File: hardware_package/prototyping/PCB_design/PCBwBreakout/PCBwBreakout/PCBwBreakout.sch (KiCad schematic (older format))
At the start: 4 parts

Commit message: Fixed Schematic frame & title, added Lora Headers
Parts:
- added ? (x2), U?: VIN, symbol PCBwBreakout-eagle-import:VIN
- added JP?: HEADER-1X5, symbol PCBwBreakout-eagle-import:HEADER-1X5
- added JP?: HEADER-1X9, symbol PCBwBreakout-eagle-import:HEADER-1X9
- added R? (x2): 100k, symbol Device:R
- ?: symbol PCBwBreakout-eagle-import:VBAT -> PCBwBreakout-rescue:VBAT-PCBwBreakout-eagle-import
- ?: symbol PCBwBreakout-eagle-import:VBUS -> PCBwBreakout-rescue:VBUS-PCBwBreakout-eagle-import
- JP?: symbol PCBwBreakout-eagle-import:HEADER-1X12 -> PCBwBreakout-rescue:HEADER-1X12-PCBwBreakout-eagle-import
- JP?: symbol PCBwBreakout-eagle-import:HEADER-1X16 -> PCBwBreakout-rescue:HEADER-1X16-PCBwBreakout-eagle-import
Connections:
- net labels added: CS_5V, DIO0, DIO1, DIO2, DIO3, DIO4, DIO5, MISO_3V, MOSI_5V, RST_5V, SCK_5V
- wire segments 30 -> 48
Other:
- note added: "RFM69HCW\n"
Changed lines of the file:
@@
 $EndDescr
 $Comp
-L PCBwBreakout-eagle-import:HEADER-1X12 JP?
+L PCBwBreakout-rescue:HEADER-1X12-PCBwBreakout-eagle-import JP?
 U 1 1 5F621D11
 P 1700 1750
@@
 $EndComp
 $Comp
-L PCBwBreakout-eagle-import:HEADER-1X16 JP?
+L PCBwBreakout-rescue:HEADER-1X16-PCBwBreakout-eagle-import JP?
 U 1 1 5F62456E
 P 3200 1800
@@
 	1600 2150 1100 2150
 $Comp
-L PCBwBreakout-eagle-import:VBAT ?
+L PCBwBreakout-rescue:VBAT-PCBwBreakout-eagle-import ?
 U 1 1 5F62F850
 P 900 1150
@@
 $EndComp
 $Comp
-L PCBwBreakout-eagle-import:VBUS ?
+L PCBwBreakout-rescue:VBUS-PCBwBreakout-eagle-import ?
 U 1 1 5F630C46
 P 900 1350
@@
 Wire Notes Line
 	500  3100 4100 3100
-Wire Notes Line
-	4100 3100 4100 500
 Text Notes 600  600  0    71   ~ 0
 Feather Headers\n
+$Comp
+L PCBwBreakout-eagle-import:HEADER-1X5 JP?
+U 1 1 5F60BB99
+P 1750 4000
+F 0 "JP?" H 1828 4053 59  0000 L CNN
+F 1 "HEADER-1X5" H 1828 3948 59  0000 L CNN
+F 2 "" H 1750 4000 71  0001 C CNN
+F 3 "" H 1750 4000 71  0001 C CNN
+	1    1750 4000
+	1    0    0    -1
+$EndComp
+Wire Wire Line
+	1650 3800 1100 3800
+Wire Wire Line
+	1650 3900 1100 3900
+Wire Wire Line
+	1650 4000 1100 4000
+Wire Wire Line
+	1650 4100 1100 4100
+Wire Wire Line
+	1650 4200 1100 4200
+Text Label 1200 3800 0    71   ~ 0
+DIO1
+Text Label 1200 3900 0    71   ~ 0
+DIO2
+Text Label 1200 4000 0    71   ~ 0
+DIO3
+Text Label 1200 4100 0    71   ~ 0
+DIO4
+Text Label 1200 4200 0    71   ~ 0
+DIO5
+$Comp
+L PCBwBreakout-eagle-import:HEADER-1X9 JP?
+U 1 1 5F613941
+P 3300 3850
+F 0 "JP?" H 3378 3903 59  0000 L CNN
+F 1 "HEADER-1X9" H 3378 3798 59  0000 L CNN
+F 2 "" H 3300 3850 71  0001 C CNN
+F 3 "" H 3300 3850 71  0001 C CNN
+	1    3300 3850
+	1    0    0    -1
+$EndComp
+$Comp
+L PCBwBreakout-eagle-import:VIN ?
+U 1 1 5F61445D
+P 2500 3450
+F 0 "?" H 2550 3500 71  0001 C CNN
+F 1 "VIN" V 2617 3413 42  0000 C CNN
+F 2 "" H 2500 3450 71  0001 C CNN
+F 3 "" H 2500 3450 71  0001 C CNN
+	1    2500 3450
+	0    -1   -1   0
+$EndComp
+Wire Wire Line
+	3200 3450 2600 3450
+$Comp
+L power:GND #PWR?
+U 1 1 5F615E5F
+P 2700 3550
+F 0 "#PWR?" H 2700 3300 50  0001 C CNN
+F 1 "GND" V 2705 3422 50  0000 R CNN
+F 2 "" H 2700 3550 50  0001 C CNN
+F 3 "" H 2700 3550 50  0001 C CNN
+	1    2700 3550
+	0    1    1    0
+$EndComp
+Wire Wire Line
+	3200 3550 2700 3550
+Text Label 2800 3650 0    71   ~ 0
+EN
+Text Label 2750 3750 0    71   ~ 0
+DIO0
+Text Label 2650 3850 0    71   ~ 0
+SCK_5V
+Text Label 2600 3950 0    71   ~ 0
+MISO_3V
+Wire Wire Line
+	2550 3950 3200 3950
+Wire Wire Line
+	2550 3850 3200 3850
+Wire Wire Line
+	2550 3750 3200 3750
+Wire Wire Line
+	2550 3650 3200 3650
+Wire Wire Line
+	2550 4050 3200 4050
+Text Label 2600 4050 0    71   ~ 0
+MOSI_5V
+$Comp
+L Device:R R?
+U 1 1 5F622386
+P 2500 4500
+F 0 "R?" H 2570 4546 50  0000 L CNN
+F 1 "100k" H 2570 4455 50  0000 L CNN
+F 2 "" V 2430 4500 50  0001 C CNN
+F 3 "~" H 2500 4500 50  0001 C CNN
+	1    2500 4500
+	1    0    0    -1
+$EndComp
+$Comp
+L Device:R R?
+U 1 1 5F6265FE
+P 2800 4500
+F 0 "R?" H 2870 4546 50  0000 L CNN
+F 1 "100k" H 2870 4455 50  0000 L CNN
+F 2 "" V 2730 4500 50  0001 C CNN
+F 3 "~" H 2800 4500 50  0001 C CNN
+	1    2800 4500
+	1    0    0    -1
+$EndComp
+Wire Wire Line
+	3200 4150 2500 4150
+Wire Wire Line
+	2500 4150 2500 4350
+Wire Wire Line
+	3200 4250 2800 4250
+Wire Wire Line
+	2800 4250 2800 4350
+$Comp
+L PCBwBreakout-eagle-import:VIN ?
+U 1 1 5F628E28
+P 2500 4850
+F 0 "?" H 2550 4900 71  0001 C CNN
+F 1 "VIN" H 2422 4812 42  0000 R CNN
+F 2 "" H 2500 4850 71  0001 C CNN
+F 3 "" H 2500 4850 71  0001 C CNN
+	1    2500 4850
+	-1   0    0    1
+$EndComp
+$Comp
+L PCBwBreakout-eagle-import:VIN U?
+U 1 1 5F629B04
+P 2800 4850
+F 0 "U?" H 2850 4900 71  0001 C CNN
+F 1 "VIN" H 2722 4812 42  0000 R CNN
+F 2 "" H 2800 4850 71  0001 C CNN
+F 3 "" H 2800 4850 71  0001 C CNN
+	1    2800 4850
+	-1   0    0    1
+$EndComp
+Wire Wire Line
+	2500 4650 2500 4750
+Wire Wire Line
+	2800 4650 2800 4750
+Text Label 2650 4150 0    71   ~ 0
+CS_5V
+Text Label 2800 4250 0    71   ~ 0
+RST_5V
+Wire Notes Line
+	450  5150 4100 5150
+Wire Notes Line
+	4100 500  4100 5150
+Text Notes 550  3250 0    71   ~ 0
+RFM69HCW\n
 $EndSCHEMATC

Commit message: Added GPS headers
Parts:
- added ? (x2): 3.3V, symbol PCBwBreakout-eagle-import:3.3V
- added JP? (x2): HEADER-1X6, symbol PCBwBreakout-eagle-import:HEADER-1X6
- ? (x2), U?: symbol PCBwBreakout-eagle-import:VIN -> PCBwBreakout-rescue:VIN-PCBwBreakout-eagle-import
- JP?: symbol PCBwBreakout-eagle-import:HEADER-1X5 -> PCBwBreakout-rescue:HEADER-1X5-PCBwBreakout-eagle-import
- JP?: symbol PCBwBreakout-eagle-import:HEADER-1X9 -> PCBwBreakout-rescue:HEADER-1X9-PCBwBreakout-eagle-import
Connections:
- net labels added: 1PPS, RXI, TXO, VCC, WAKEUP
- net labels removed: +3V3
- wire segments 48 -> 61
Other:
- note added: "GPS \n"
- note added: "STM32 Adafruit Feather\n\n"
- note removed: "Feather Headers\n"
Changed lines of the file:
@@
 Wire Wire Line
 	3100 2500 2900 2500
-Text Label 2600 2500 0    50   ~ 0
-+3V3
 Wire Wire Line
 	2900 2400 2900 2500
@@
 Wire Notes Line
 	500  3100 4100 3100
-Text Notes 600  600  0    71   ~ 0
-Feather Headers\n
-$Comp
-L PCBwBreakout-eagle-import:HEADER-1X5 JP?
+Text Notes 600  700  0    71   ~ 0
+STM32 Adafruit Feather\n\n
+$Comp
+L PCBwBreakout-rescue:HEADER-1X5-PCBwBreakout-eagle-import JP?
 U 1 1 5F60BB99
 P 1750 4000
@@
 DIO5
 $Comp
-L PCBwBreakout-eagle-import:HEADER-1X9 JP?
+L PCBwBreakout-rescue:HEADER-1X9-PCBwBreakout-eagle-import JP?
 U 1 1 5F613941
 P 3300 3850
@@
 $EndComp
 $Comp
-L PCBwBreakout-eagle-import:VIN ?
+L PCBwBreakout-rescue:VIN-PCBwBreakout-eagle-import ?
 U 1 1 5F61445D
 P 2500 3450
@@
 	2800 4250 2800 4350
 $Comp
-L PCBwBreakout-eagle-import:VIN ?
+L PCBwBreakout-rescue:VIN-PCBwBreakout-eagle-import ?
 U 1 1 5F628E28
 P 2500 4850
@@
 $EndComp
 $Comp
-L PCBwBreakout-eagle-import:VIN U?
+L PCBwBreakout-rescue:VIN-PCBwBreakout-eagle-import U?
 U 1 1 5F629B04
 P 2800 4850
@@
 Text Label 2800 4250 0    71   ~ 0
 RST_5V
+Text Notes 550  3250 0    71   ~ 0
+RFM69HCW\n
+$Comp
+L PCBwBreakout-eagle-import:3.3V ?
+U 1 1 5F660521
+P 2400 2500
+F 0 "?" H 2450 2550 71  0001 C CNN
+F 1 "3.3V" V 2517 2463 42  0000 C CNN
+F 2 "" H 2400 2500 71  0001 C CNN
+F 3 "" H 2400 2500 71  0001 C CNN
+	1    2400 2500
+	0    -1   -1   0
+$EndComp
+Text Label 850  6200 0    71   ~ 0
+~RESET~
+Text Label 950  6100 0    71   ~ 0
+SDA
+Text Label 950  6000 0    71   ~ 0
+SCL
+Wire Wire Line
+	1400 6200 800  6200
+Wire Wire Line
+	1400 6100 800  6100
+Wire Wire Line
+	1400 6000 800  6000
+Wire Wire Line
+	900  5900 1400 5900
+$Comp
+L power:GND #PWR?
+U 1 1 5F665743
+P 900 5900
+F 0 "#PWR?" H 900 5650 50  0001 C CNN
+F 1 "GND" V 905 5772 50  0000 R CNN
+F 2 "" H 900 5900 50  0001 C CNN
+F 3 "" H 900 5900 50  0001 C CNN
+	1    900  5900
+	0    1    1    0
+$EndComp
+Wire Wire Line
+	750  5800 1400 5800
+$Comp
+L PCBwBreakout-eagle-import:3.3V ?
+U 1 1 5F65D5C2
+P 650 5800
+F 0 "?" H 700 5850 71  0001 C CNN
+F 1 "3.3V" V 767 5763 42  0000 C CNN
+F 2 "" H 650 5800 71  0001 C CNN
+F 3 "" H 650 5800 71  0001 C CNN
+	1    650  5800
+	0    -1   -1   0
+$EndComp
+Wire Wire Line
+	850  5700 1400 5700
+Wire Wire Line
+	850  5600 850  5700
+$Comp
+L PCBwBreakout-eagle-import:VCC #P+?
+U 1 1 5F658A43
+P 850 5500
+F 0 "#P+?" H 850 5500 71  0001 C CNN
+F 1 "VCC" H 850 5622 59  0000 C CNN
+F 2 "" H 850 5500 71  0001 C CNN
+F 3 "" H 850 5500 71  0001 C CNN
+	1    850  5500
+	1    0    0    -1
+$EndComp
+$Comp
+L PCBwBreakout-eagle-import:HEADER-1X6 JP?
+U 1 1 5F6558D8
+P 1500 6000
+F 0 "JP?" H 1578 6103 59  0000 L CNN
+F 1 "HEADER-1X6" H 1578 5998 59  0000 L CNN
+F 2 "" H 1500 6000 71  0001 C CNN
+F 3 "" H 1500 6000 71  0001 C CNN
+	1    1500 6000
+	1    0    0    -1
+$EndComp
 Wire Notes Line
 	450  5150 4100 5150
+$Comp
+L PCBwBreakout-eagle-import:HEADER-1X6 JP?
+U 1 1 5F675AA7
+P 3300 6000
+F 0 "JP?" H 3378 6103 59  0000 L CNN
+F 1 "HEADER-1X6" H 3378 5998 59  0000 L CNN
+F 2 "" H 3300 6000 71  0001 C CNN
+F 3 "" H 3300 6000 71  0001 C CNN
+	1    3300 6000
+	1    0    0    -1
+$EndComp
+$Comp
+L power:GND #PWR?
+U 1 1 5F677526
+P 2500 5700
+F 0 "#PWR?" H 2500 5450 50  0001 C CNN
+F 1 "GND" V 2505 5572 50  0000 R CNN
+F 2 "" H 2500 5700 50  0001 C CNN
+F 3 "" H 2500 5700 50  0001 C CNN
+	1    2500 5700
+	0    1    1    0
+$EndComp
+Wire Wire Line
+	3200 5700 2500 5700
+Wire Wire Line
+	3200 5800 2500 5800
+Wire Wire Line
+	3200 5900 2500 5900
+Wire Wire Line
+	3200 6000 2500 6000
+Wire Wire Line
+	3200 6100 2500 6100
+Wire Wire Line
+	3200 6200 2500 6200
+Text Label 2650 5800 0    71   ~ 0
+1PPS
+$Comp
+L PCBwBreakout-eagle-import:VCC #P+?
+U 1 1 5F68239E
+P 2400 5900
+F 0 "#P+?" H 2400 5900 71  0001 C CNN
+F 1 "VCC" V 2400 5969 59  0000 L CNN
+F 2 "" H 2400 5900 71  0001 C CNN
+F 3 "" H 2400 5900 71  0001 C CNN
+	1    2400 5900
+	0    -1   -1   0
+$EndComp
+Text Label 2700 6000 0    71   ~ 0
+RXI
+Text Label 2700 6100 0    71   ~ 0
+TXO
+Text Label 2600 6200 0    71   ~ 0
+WAKEUP
 Wire Notes Line
-	4100 500  4100 5150
-Text Notes 550  3250 0    71   ~ 0
-RFM69HCW\n
+	450  6500 4100 6500
+Wire Notes Line
+	4100 500  4100 6500
+Text Notes 500  5300 0    71   ~ 0
+GPS \n
 $EndSCHEMATC

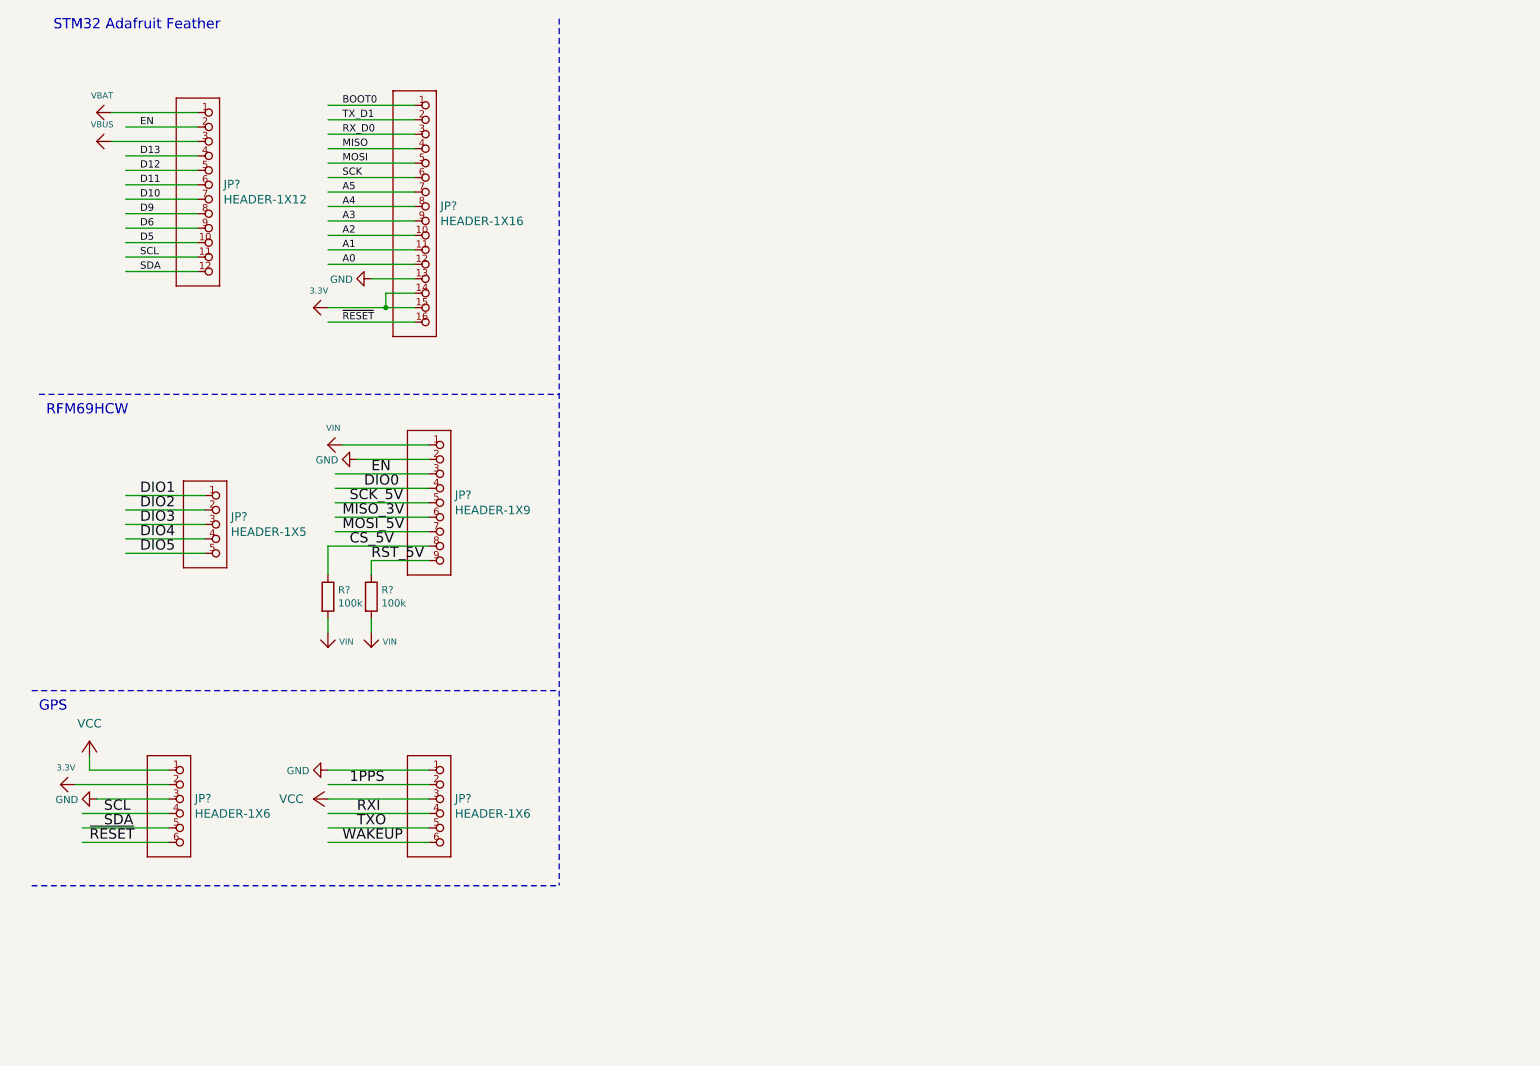
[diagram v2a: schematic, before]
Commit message: Added IMU Headers
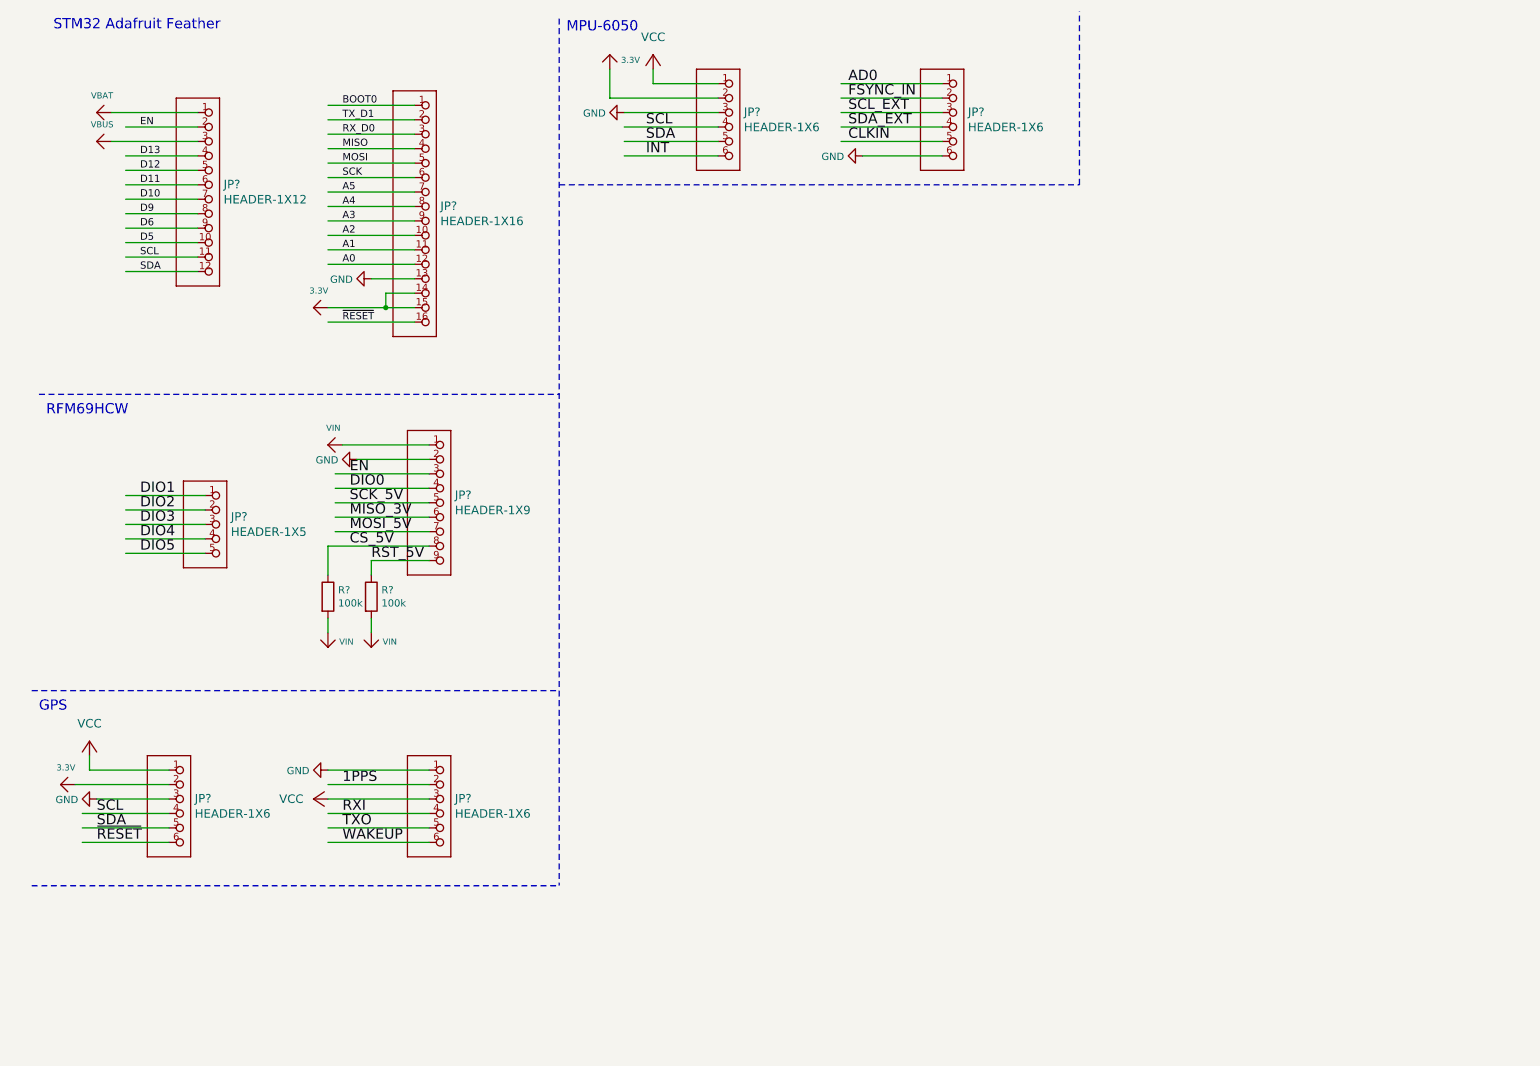
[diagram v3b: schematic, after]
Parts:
- added ?: 3.3V, symbol PCBwBreakout-eagle-import:3.3V
- added JP? (x2): HEADER-1X6, symbol PCBwBreakout-eagle-import:HEADER-1X6
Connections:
- net labels added: AD0, CLKIN, FSYNC_IN, INT, SCL_EXT, SDA_EXT
- wire segments 61 -> 75
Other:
- note added: "MPU-6050\n"
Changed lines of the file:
@@
 Wire Wire Line
 	3200 3550 2700 3550
-Text Label 2800 3650 0    71   ~ 0
+Text Label 2650 3650 0    71   ~ 0
 EN
-Text Label 2750 3750 0    71   ~ 0
+Text Label 2650 3750 0    71   ~ 0
 DIO0
 Text Label 2650 3850 0    71   ~ 0
 SCK_5V
-Text Label 2600 3950 0    71   ~ 0
+Text Label 2650 3950 0    71   ~ 0
 MISO_3V
 Wire Wire Line
@@
 Wire Wire Line
 	2550 4050 3200 4050
-Text Label 2600 4050 0    71   ~ 0
+Text Label 2650 4050 0    71   ~ 0
 MOSI_5V
 $Comp
@@
 	0    -1   -1   0
 $EndComp
-Text Label 850  6200 0    71   ~ 0
+Text Label 900  6200 0    71   ~ 0
 ~RESET~
-Text Label 950  6100 0    71   ~ 0
+Text Label 900  6100 0    71   ~ 0
 SDA
-Text Label 950  6000 0    71   ~ 0
+Text Label 900  6000 0    71   ~ 0
 SCL
 Wire Wire Line
@@
 Wire Wire Line
 	3200 6200 2500 6200
-Text Label 2650 5800 0    71   ~ 0
+Text Label 2600 5800 0    71   ~ 0
 1PPS
 $Comp
@@
 	0    -1   -1   0
 $EndComp
-Text Label 2700 6000 0    71   ~ 0
+Text Label 2600 6000 0    71   ~ 0
 RXI
-Text Label 2700 6100 0    71   ~ 0
+Text Label 2600 6100 0    71   ~ 0
 TXO
 Text Label 2600 6200 0    71   ~ 0
@@
 Text Notes 500  5300 0    71   ~ 0
 GPS \n
+$Comp
+L PCBwBreakout-eagle-import:HEADER-1X6 JP?
+U 1 1 5F69AE38
+P 5300 1250
+F 0 "JP?" H 5378 1353 59  0000 L CNN
+F 1 "HEADER-1X6" H 5378 1248 59  0000 L CNN
+F 2 "" H 5300 1250 71  0001 C CNN
+F 3 "" H 5300 1250 71  0001 C CNN
+	1    5300 1250
+	1    0    0    -1
+$EndComp
+$Comp
+L PCBwBreakout-eagle-import:HEADER-1X6 JP?
+U 1 1 5F69BA80
+P 6850 1250
+F 0 "JP?" H 6928 1353 59  0000 L CNN
+F 1 "HEADER-1X6" H 6928 1248 59  0000 L CNN
+F 2 "" H 6850 1250 71  0001 C CNN
+F 3 "" H 6850 1250 71  0001 C CNN
+	1    6850 1250
+	1    0    0    -1
+$EndComp
+$Comp
+L PCBwBreakout-eagle-import:VCC #P+?
+U 1 1 5F69FFEA
+P 4750 750
+F 0 "#P+?" H 4750 750 71  0001 C CNN
+F 1 "VCC" H 4750 872 59  0000 C CNN
+F 2 "" H 4750 750 71  0001 C CNN
+F 3 "" H 4750 750 71  0001 C CNN
+	1    4750 750
+	1    0    0    -1
+$EndComp
+$Comp
+L PCBwBreakout-eagle-import:3.3V ?
+U 1 1 5F6A08C9
+P 4450 750
+F 0 "?" H 4500 800 71  0001 C CNN
+F 1 "3.3V" H 4528 713 42  0000 L CNN
+F 2 "" H 4450 750 71  0001 C CNN
+F 3 "" H 4450 750 71  0001 C CNN
+	1    4450 750
+	1    0    0    -1
+$EndComp
+$Comp
+L power:GND #PWR?
+U 1 1 5F6A166A
+P 4550 1150
+F 0 "#PWR?" H 4550 900 50  0001 C CNN
+F 1 "GND" V 4555 1022 50  0000 R CNN
+F 2 "" H 4550 1150 50  0001 C CNN
+F 3 "" H 4550 1150 50  0001 C CNN
+	1    4550 1150
+	0    1    1    0
+$EndComp
+Wire Wire Line
+	4450 850  4450 1050
+Wire Wire Line
+	4450 1050 5200 1050
+Wire Wire Line
+	4750 850  4750 950
+Wire Wire Line
+	4750 950  5200 950
+Wire Wire Line
+	4550 1150 5200 1150
+Wire Wire Line
+	5200 1250 4550 1250
+Wire Wire Line
+	5200 1350 4550 1350
+Wire Wire Line
+	5200 1450 4550 1450
+Text Label 4700 1250 0    71   ~ 0
+SCL
+Text Label 4700 1350 0    71   ~ 0
+SDA
+Text Label 4700 1450 0    71   ~ 0
+INT
+$Comp
+L power:GND #PWR?
+U 1 1 5F6AE3D2
+P 6200 1450
+F 0 "#PWR?" H 6200 1200 50  0001 C CNN
+F 1 "GND" V 6205 1322 50  0000 R CNN
+F 2 "" H 6200 1450 50  0001 C CNN
+F 3 "" H 6200 1450 50  0001 C CNN
+	1    6200 1450
+	0    1    1    0
+$EndComp
+Wire Wire Line
+	6750 1450 6200 1450
+Text Label 6100 950  0    71   ~ 0
+AD0
+Text Label 6100 1050 0    71   ~ 0
+FSYNC_IN
+Text Label 6100 1150 0    71   ~ 0
+SCL_EXT
+Text Label 6100 1250 0    71   ~ 0
+SDA_EXT
+Text Label 6100 1350 0    71   ~ 0
+CLKIN
+Wire Wire Line
+	6050 1050 6750 1050
+Wire Wire Line
+	6050 950  6750 950
+Wire Wire Line
+	6050 1150 6750 1150
+Wire Wire Line
+	6050 1250 6750 1250
+Wire Wire Line
+	6050 1350 6750 1350
+Wire Notes Line
+	4100 1650 7700 1650
+Wire Notes Line
+	7700 1650 7700 450
+Text Notes 4150 600  0    71   ~ 0
+MPU-6050\n
 $EndSCHEMATC
